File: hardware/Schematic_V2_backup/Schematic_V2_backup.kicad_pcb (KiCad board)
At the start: 2 copper layers, 193.2 x 111.3 mm, 196 parts, among them IC1 RTC_DS3231M, IC2 SIM7600CE-H, J1 USB_C_Receptacle_USB2.0_14P, J10 ANT_LTE, J11 ANT_LTE, J12 ANT_LTE, J14 SIM7100-6pin-socket-smd, J15 Screw_Terminal_01x04, J17 HR911105A, J3 Screw_Terminal_01x03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

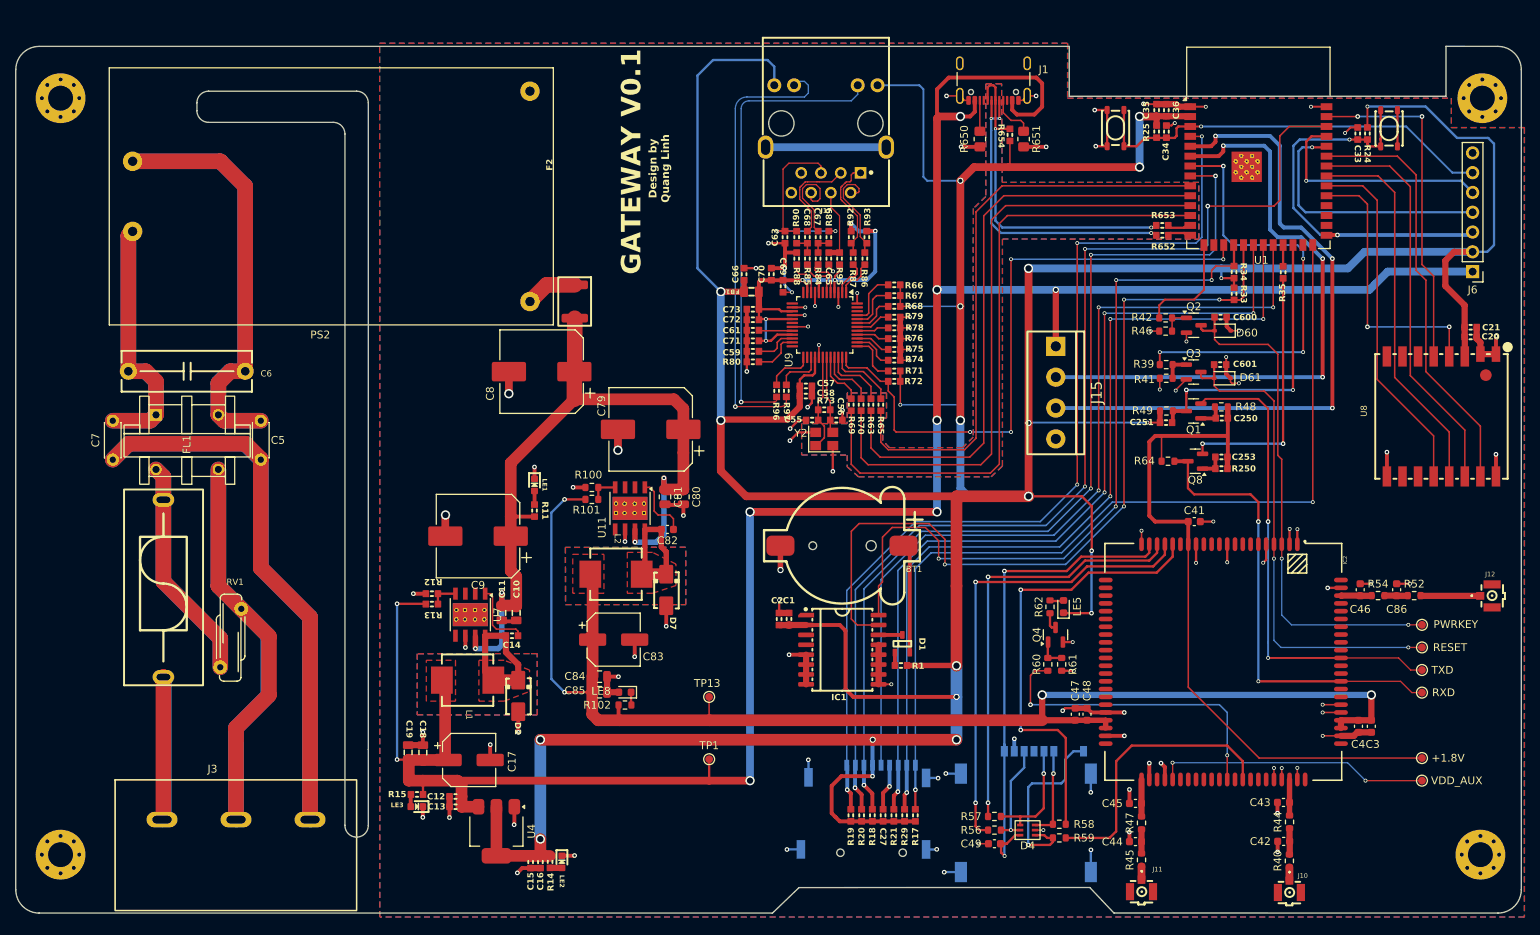
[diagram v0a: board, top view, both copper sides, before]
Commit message: Update PCB Layout for Gateway, 23/3/2026
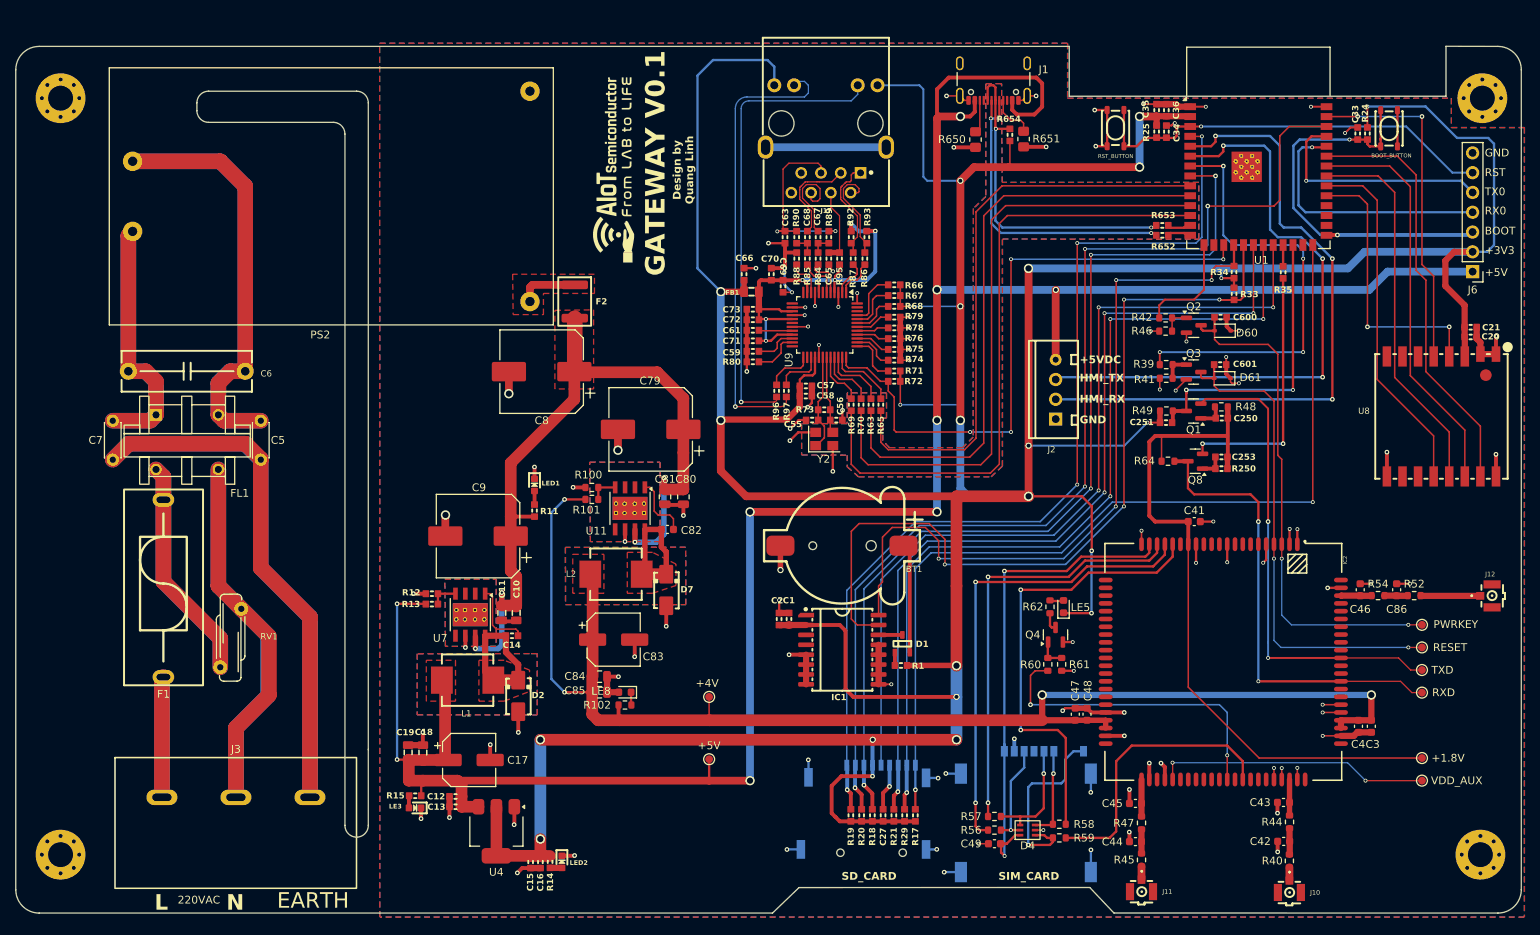
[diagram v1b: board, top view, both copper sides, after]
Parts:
- removed J15: Screw_Terminal_01x04, IVS_NEW_FOOTPRINT:Terminal_HT-3.96mm-4P-Horizontal-Pluggable
- added G***: LOGO, logolab:Logolab_new_24x5.6mm, F.Cu at (207.0, 157.3)
- added J2: Conn_01x04_Pin, IVS_NEW_FOOTPRINT:Conn_XH-P2.54mm-4P, F.Cu at (263.7, 185.5)
- moved J3 2.86 mm to (158.5, 241.2)
- moved R650 0.56 mm to (253.4, 153.5)
- moved LE3 0.29 mm to (181.5, 239.3)
- moved R15 0.29 mm to (181.5, 237.7)
- renumbered TP13 to +4V, TP1 to +5V, LE1 to LED1, LE2 to LED2
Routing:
- net /Khối nguồn/L: track 37.3 -> 31.0 mm
- net /Khối nguồn/N: track 98.7 -> 93.0 mm
- net Earth: track 139.1 -> 133.4 mm
- net +3.3V: track 631.4 -> 635.5 mm
- net +12V: track 100.9 -> 103.2 mm
- net +5V: track 317.3 -> 319.1 mm
- net /ESP32-S3/ESP_HMI_TX: track 86.3 -> 85.2 mm
- net /Khối nguồn/fuse: track 6.64 -> 7.70 mm
- net /ESP32-S3/ESP_HMI_RX: track 79.3 -> 80.0 mm
- added copper zone on F.Cu, net +12V
- added copper zone on F.Cu, net /Khối nguồn/fuse
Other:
- board text added: "+3V3"
- board text added: "+5V"
- board text added: "+5VDC"
- board text added: "220VAC"
- board text added: "BOOT"
- board text added: "BOOT_BUTTON"
- board text added: "EARTH"
- board text added: "GND"
- board text added: "HMI_RX"
- board text added: "HMI_TX"
- board text added: "L"
- board text added: "N"
- board text added: "RST"
- board text added: "RST_BUTTON"
- board text added: "RX0"
- board text added: "SD_CARD"
- board text added: "SIM_CARD"
- board text added: "TX0"
